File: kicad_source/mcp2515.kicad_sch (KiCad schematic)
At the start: 14 parts, among them CN4 GH_SM04B-GHS-TB, CN5 GH_SM04B-GHS-TB, U8 MCP2515, U9 SN65HVD232, Y1 16MHz

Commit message: started first placement
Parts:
- renumbered C3 to C5, C7 to C6, C8 to C7, C4 to C8, CN4 to CN10, CN5 to CN11, D2 to D3, R1 to R23, R2 to R24, R3 to R25, U8 to U2, U9 to U3
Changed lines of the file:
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@@
   (symbol (lib_id "OpenCyphalPicoBase-rescue:MCP2515-IC_transceiver_can") (at 127 55.88 0) (unit 1)
     (in_bom yes) (on_board yes)
-    (property "Reference" "U8" (id 0) (at 127 37.465 0))
+    (property "Reference" "U2" (id 0) (at 127 37.465 0))
     (property "Value" "MCP2515" (id 1) (at 127 39.7764 0))
     (property "Footprint" "Package_SO:SOIC-18W_7.5x11.6mm_P1.27mm" (id 2) (at 127 55.88 0)
@@
   (symbol (lib_id "Device:C_Small") (at 162.56 46.99 0) (unit 1)
     (in_bom yes) (on_board yes)
-    (property "Reference" "C3" (id 0) (at 164.8968 45.8216 0)
+    (property "Reference" "C5" (id 0) (at 164.8968 45.8216 0)
       (effects (font (size 1.27 1.27)) (justify left))
     )
@@
   (symbol (lib_id "OpenCyphalPicoBase-rescue:+3.3V-power-supply") (at 162.56 41.91 0) (unit 1)
     (in_bom yes) (on_board yes)
-    (property "Reference" "#PWR025" (id 0) (at 162.56 45.72 0)
+    (property "Reference" "#PWR052" (id 0) (at 162.56 45.72 0)
       (effects (font (size 1.27 1.27)) hide)
     )
@@
   (symbol (lib_id "OpenCyphalPicoBase-rescue:GND-power-supply") (at 162.56 50.8 0) (unit 1)
     (in_bom yes) (on_board yes)
-    (property "Reference" "#PWR026" (id 0) (at 162.56 57.15 0)
+    (property "Reference" "#PWR053" (id 0) (at 162.56 57.15 0)
       (effects (font (size 1.27 1.27)) hide)
     )
@@
   (symbol (lib_id "OpenCyphalPicoBase-rescue:GND-power-supply") (at 170.18 86.36 0) (unit 1)
     (in_bom yes) (on_board yes)
-    (property "Reference" "#PWR027" (id 0) (at 170.18 92.71 0)
+    (property "Reference" "#PWR055" (id 0) (at 170.18 92.71 0)
       (effects (font (size 1.27 1.27)) hide)
     )
@@
   (symbol (lib_id "Device:R_Small") (at 87.63 38.1 0) (unit 1)
     (in_bom yes) (on_board yes)
-    (property "Reference" "R3" (id 0) (at 89.1286 36.9316 0)
+    (property "Reference" "R25" (id 0) (at 89.1286 36.9316 0)
       (effects (font (size 1.27 1.27)) (justify left))
     )
@@
   (symbol (lib_id "OpenCyphalPicoBase-rescue:+3.3V-power-supply") (at 87.63 34.29 0) (unit 1)
     (in_bom yes) (on_board yes)
-    (property "Reference" "#PWR024" (id 0) (at 87.63 38.1 0)
+    (property "Reference" "#PWR051" (id 0) (at 87.63 38.1 0)
       (effects (font (size 1.27 1.27)) hide)
     )
@@
   (symbol (lib_id "Device:R_Small") (at 80.01 38.1 0) (unit 1)
     (in_bom yes) (on_board yes)
-    (property "Reference" "R2" (id 0) (at 81.5086 36.9316 0)
+    (property "Reference" "R24" (id 0) (at 81.5086 36.9316 0)
       (effects (font (size 1.27 1.27)) (justify left))
     )
@@
   (symbol (lib_id "OpenCyphalPicoBase-rescue:+3.3V-power-supply") (at 80.01 34.29 0) (unit 1)
     (in_bom yes) (on_board yes)
-    (property "Reference" "#PWR023" (id 0) (at 80.01 38.1 0)
+    (property "Reference" "#PWR050" (id 0) (at 80.01 38.1 0)
       (effects (font (size 1.27 1.27)) hide)
     )
@@
   (symbol (lib_id "Device:R_Small") (at 72.39 38.1 0) (unit 1)
     (in_bom yes) (on_board yes)
-    (property "Reference" "R1" (id 0) (at 73.8886 36.9316 0)
+    (property "Reference" "R23" (id 0) (at 73.8886 36.9316 0)
       (effects (font (size 1.27 1.27)) (justify left))
     )
@@
   (symbol (lib_id "OpenCyphalPicoBase-rescue:+3.3V-power-supply") (at 72.39 34.29 0) (unit 1)
     (in_bom yes) (on_board yes)
-    (property "Reference" "#PWR022" (id 0) (at 72.39 38.1 0)
+    (property "Reference" "#PWR049" (id 0) (at 72.39 38.1 0)
       (effects (font (size 1.27 1.27)) hide)
     )
@@
   (symbol (lib_id "OpenCyphalPicoBase-rescue:SN65HVD232-CAN-transceiver") (at 210.82 66.04 0) (unit 1)
     (in_bom yes) (on_board yes)
-    (property "Reference" "U9" (id 0) (at 224.155 43.5102 0)
+    (property "Reference" "U3" (id 0) (at 224.155 43.5102 0)
       (effects (font (size 1.524 1.524)))
     )
@@
   (symbol (lib_id "Device:C_Small") (at 198.12 45.72 0) (unit 1)
     (in_bom yes) (on_board yes)
-    (property "Reference" "C4" (id 0) (at 200.4568 44.5516 0)
+    (property "Reference" "C8" (id 0) (at 200.4568 44.5516 0)
       (effects (font (size 1.27 1.27)) (justify left))
     )
@@
   (symbol (lib_id "OpenCyphalPicoBase-rescue:+3.3V-power-supply") (at 198.12 40.64 0) (unit 1)
     (in_bom yes) (on_board yes)
-    (property "Reference" "#PWR028" (id 0) (at 198.12 44.45 0)
+    (property "Reference" "#PWR058" (id 0) (at 198.12 44.45 0)
       (effects (font (size 1.27 1.27)) hide)
     )
@@
   (symbol (lib_id "OpenCyphalPicoBase-rescue:GND-power-supply") (at 198.12 49.53 0) (unit 1)
     (in_bom yes) (on_board yes)
-    (property "Reference" "#PWR029" (id 0) (at 198.12 55.88 0)
+    (property "Reference" "#PWR059" (id 0) (at 198.12 55.88 0)
       (effects (font (size 1.27 1.27)) hide)
     )
@@
   (symbol (lib_id "OpenCyphalPicoBase-rescue:GND-power-supply") (at 209.55 63.5 0) (unit 1)
     (in_bom yes) (on_board yes)
-    (property "Reference" "#PWR030" (id 0) (at 209.55 69.85 0)
+    (property "Reference" "#PWR060" (id 0) (at 209.55 69.85 0)
       (effects (font (size 1.27 1.27)) hide)
     )
@@
   (symbol (lib_id "OpenCyphalPicoBase-rescue:CONN_01X04-mechanical-connectors") (at 223.52 106.68 0) (unit 1)
     (in_bom yes) (on_board yes)
-    (property "Reference" "CN4" (id 0) (at 225.5012 105.6386 0)
+    (property "Reference" "CN10" (id 0) (at 225.5012 105.6386 0)
       (effects (font (size 1.27 1.27)) (justify left))
     )
@@
   (symbol (lib_id "OpenCyphalPicoBase-rescue:GND-power-supply") (at 215.9 113.03 0) (unit 1)
     (in_bom yes) (on_board yes)
-    (property "Reference" "#PWR036" (id 0) (at 215.9 119.38 0)
+    (property "Reference" "#PWR061" (id 0) (at 215.9 119.38 0)
       (effects (font (size 1.27 1.27)) hide)
     )
@@
   (symbol (lib_id "OpenCyphalPicoBase-rescue:CONN_01X04-mechanical-connectors") (at 223.52 130.81 0) (unit 1)
     (in_bom yes) (on_board yes)
-    (property "Reference" "CN5" (id 0) (at 225.5012 129.7686 0)
+    (property "Reference" "CN11" (id 0) (at 225.5012 129.7686 0)
       (effects (font (size 1.27 1.27)) (justify left))
     )
@@
   (symbol (lib_id "OpenCyphalPicoBase-rescue:GND-power-supply") (at 215.9 137.16 0) (unit 1)
     (in_bom yes) (on_board yes)
-    (property "Reference" "#PWR037" (id 0) (at 215.9 143.51 0)
+    (property "Reference" "#PWR062" (id 0) (at 215.9 143.51 0)
       (effects (font (size 1.27 1.27)) hide)
     )
@@
   (symbol (lib_id "Device:D_Schottky_Small") (at 220.98 156.21 0) (unit 1)
     (in_bom yes) (on_board yes)
-    (property "Reference" "D2" (id 0) (at 220.98 151.003 0))
+    (property "Reference" "D3" (id 0) (at 220.98 151.003 0))
     (property "Value" "MBR0530T1G" (id 1) (at 220.98 153.3144 0))
     (property "Footprint" "Diode_SMD:D_SOD-123" (id 2) (at 220.98 156.21 90)
@@
   (symbol (lib_id "Device:C_Small") (at 176.53 85.09 0) (unit 1)
     (in_bom yes) (on_board yes)
-    (property "Reference" "C8" (id 0) (at 178.8668 83.9216 0)
+    (property "Reference" "C7" (id 0) (at 178.8668 83.9216 0)
       (effects (font (size 1.27 1.27)) (justify left))
     )
@@
   (symbol (lib_id "Device:C_Small") (at 163.83 85.09 0) (mirror y) (unit 1)
     (in_bom yes) (on_board yes)
-    (property "Reference" "C7" (id 0) (at 161.4932 83.9216 0)
+    (property "Reference" "C6" (id 0) (at 161.4932 83.9216 0)
       (effects (font (size 1.27 1.27)) (justify left))
     )
@@
   (symbol (lib_id "OpenCyphalPicoBase-rescue:GND-power-supply") (at 163.83 88.9 0) (unit 1)
     (in_bom yes) (on_board yes)
-    (property "Reference" "#PWR034" (id 0) (at 163.83 95.25 0)
+    (property "Reference" "#PWR054" (id 0) (at 163.83 95.25 0)
       (effects (font (size 1.27 1.27)) hide)
     )
@@
   (symbol (lib_id "OpenCyphalPicoBase-rescue:GND-power-supply") (at 176.53 88.9 0) (unit 1)
     (in_bom yes) (on_board yes)
-    (property "Reference" "#PWR035" (id 0) (at 176.53 95.25 0)
+    (property "Reference" "#PWR056" (id 0) (at 176.53 95.25 0)
       (effects (font (size 1.27 1.27)) hide)
     )
@@
   (symbol (lib_id "OpenCyphalPicoBase-rescue:GND-power-supply") (at 243.84 45.72 0) (unit 1)
     (in_bom yes) (on_board yes)
-    (property "Reference" "#PWR0102" (id 0) (at 243.84 52.07 0)
+    (property "Reference" "#PWR063" (id 0) (at 243.84 52.07 0)
       (effects (font (size 1.27 1.27)) hide)
     )
@@
   (symbol (lib_id "power:+5V") (at 195.58 154.94 0) (unit 1)
     (in_bom yes) (on_board yes) (fields_autoplaced)
-    (property "Reference" "#PWR?" (id 0) (at 195.58 158.75 0)
-      (effects (font (size 1.27 1.27)) hide)
-    )
+    (property "Reference" "#PWR057" (id 0) (at 195.58 158.75 0)
+      (effects (font (size 1.27 1.27)) hide)
+    )

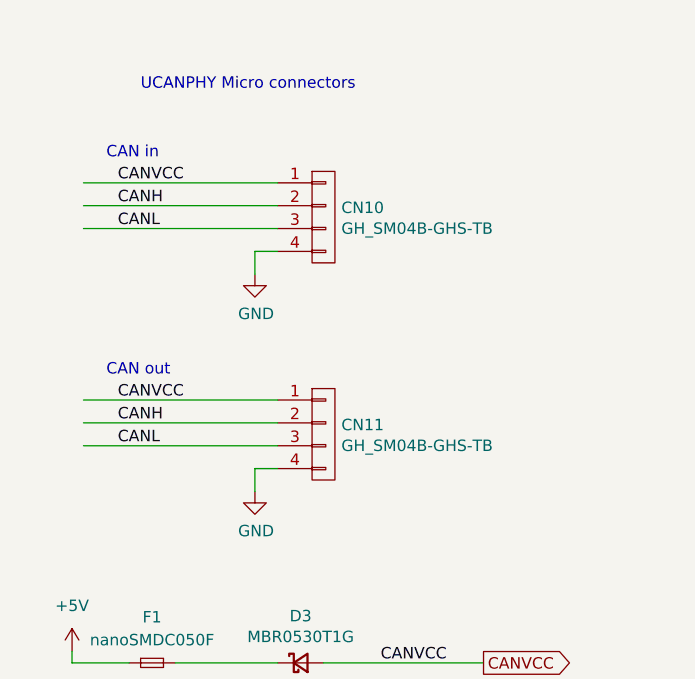
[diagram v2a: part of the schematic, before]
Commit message: added mounting pads, beautified layout, run DRC
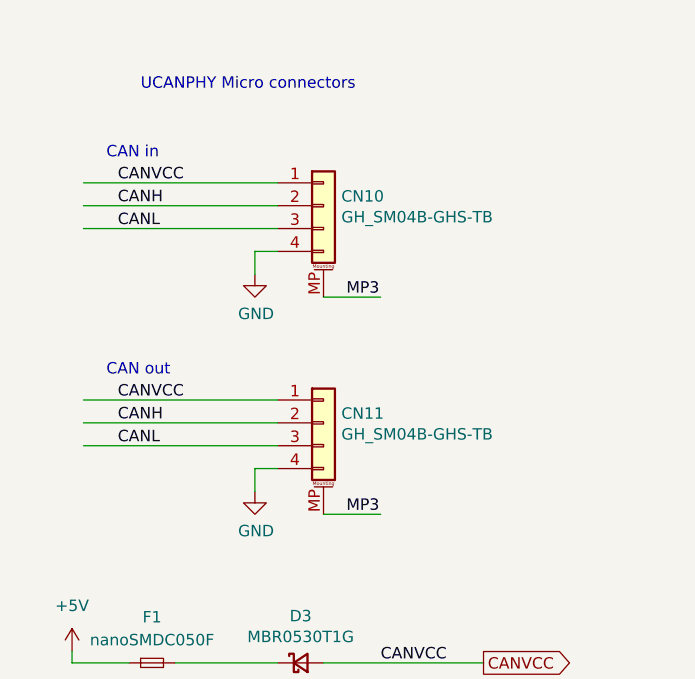
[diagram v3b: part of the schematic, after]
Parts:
- CN10, CN11: symbol OpenCyphalPicoBase-rescue:CONN_01X04-mechanical-connectors -> Connector_Generic_MountingPin:Conn_01x04_MountingPin
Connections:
- new net MP3: CN10.MP (MountPin), CN11.MP (MountPin)
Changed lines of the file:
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@@
   (title_block
     (title "OpenCyphalServoController12")
-    (date "2023-02-03")
+    (date "2023-02-04")
     (rev "0.1")
     (company "generationmake")
@@
     (stroke (width 0) (type default) (color 0 0 0 0))
   )
+  (wire (pts (xy 223.52 115.57) (xy 229.87 115.57))
+    (stroke (width 0) (type default) (color 0 0 0 0))
+  )
   (wire (pts (xy 162.56 50.8) (xy 162.56 49.53))
     (stroke (width 0) (type default) (color 0 0 0 0))
@@
     (stroke (width 0) (type default) (color 0 0 0 0))
   )
+  (wire (pts (xy 223.52 139.7) (xy 229.87 139.7))
+    (stroke (width 0) (type default) (color 0 0 0 0))
+  )
   (wire (pts (xy 91.44 58.42) (xy 113.03 58.42))
     (stroke (width 0) (type default) (color 0 0 0 0))
@@
     (effects (font (size 1.27 1.27)) (justify left bottom))
   )
+  (label "MP3" (at 226.06 115.57 0)
+    (effects (font (size 1.27 1.27)) (justify left bottom))
+  )
   (label "MCP2515_TX2RTS" (at 92.71 68.58 0)
     (effects (font (size 1.27 1.27)) (justify left bottom))
@@
   )
   (label "MOSI" (at 92.71 50.8 0)
+    (effects (font (size 1.27 1.27)) (justify left bottom))
+  )
+  (label "MP3" (at 226.06 139.7 0)
     (effects (font (size 1.27 1.27)) (justify left bottom))
   )
@@
     (pin "1")
   )
-  (symbol (lib_id "OpenCyphalPicoBase-rescue:CONN_01X04-mechanical-connectors") (at 223.52 106.68 0) (unit 1)
-    (in_bom yes) (on_board yes)
-    (property "Reference" "CN10" (id 0) (at 225.5012 105.6386 0)
-      (effects (font (size 1.27 1.27)) (justify left))
-    )
-    (property "Value" "GH_SM04B-GHS-TB" (id 1) (at 225.5012 107.95 0)
-      (effects (font (size 1.27 1.27)) (justify left))
-    )
-    (property "Footprint" "Connector_JST:JST_GH_SM04B-GHS-TB_1x04-1MP_P1.25mm_Horizontal" (id 2) (at 223.52 106.68 0)
-      (effects (font (size 1.27 1.27)) hide)
-    )
-    (property "Datasheet" "" (id 3) (at 223.52 106.68 0))
+  (symbol (lib_id "Connector_Generic_MountingPin:Conn_01x04_MountingPin") (at 223.52 105.41 0) (unit 1)
+    (in_bom yes) (on_board yes)
+    (property "Reference" "CN10" (id 0) (at 225.5012 104.3686 0)
+      (effects (font (size 1.27 1.27)) (justify left))
+    )
+    (property "Value" "GH_SM04B-GHS-TB" (id 1) (at 225.5012 106.68 0)
+      (effects (font (size 1.27 1.27)) (justify left))
+    )
+    (property "Footprint" "Connector_JST:JST_GH_SM04B-GHS-TB_1x04-1MP_P1.25mm_Horizontal" (id 2) (at 223.52 105.41 0)
+      (effects (font (size 1.27 1.27)) hide)
+    )
+    (property "Datasheet" "~" (id 3) (at 223.52 105.41 0)
+      (effects (font (size 1.27 1.27)) hide)
+    )
     (pin "1")
     (pin "2")
     (pin "3")
     (pin "4")
+    (pin "MP")
   )
   (symbol (lib_id "OpenCyphalPicoBase-rescue:GND-power-supply") (at 215.9 113.03 0) (unit 1)
@@
     (pin "1")
   )
-  (symbol (lib_id "OpenCyphalPicoBase-rescue:CONN_01X04-mechanical-connectors") (at 223.52 130.81 0) (unit 1)
-    (in_bom yes) (on_board yes)
-    (property "Reference" "CN11" (id 0) (at 225.5012 129.7686 0)
-      (effects (font (size 1.27 1.27)) (justify left))
-    )
-    (property "Value" "GH_SM04B-GHS-TB" (id 1) (at 225.5012 132.08 0)
-      (effects (font (size 1.27 1.27)) (justify left))
-    )
-    (property "Footprint" "Connector_JST:JST_GH_SM04B-GHS-TB_1x04-1MP_P1.25mm_Horizontal" (id 2) (at 223.52 130.81 0)
-      (effects (font (size 1.27 1.27)) hide)
-    )
-    (property "Datasheet" "" (id 3) (at 223.52 130.81 0))
+  (symbol (lib_id "Connector_Generic_MountingPin:Conn_01x04_MountingPin") (at 223.52 129.54 0) (unit 1)
+    (in_bom yes) (on_board yes)
+    (property "Reference" "CN11" (id 0) (at 225.5012 128.4986 0)
+      (effects (font (size 1.27 1.27)) (justify left))
+    )
+    (property "Value" "GH_SM04B-GHS-TB" (id 1) (at 225.5012 130.81 0)
+      (effects (font (size 1.27 1.27)) (justify left))
+    )
+    (property "Footprint" "Connector_JST:JST_GH_SM04B-GHS-TB_1x04-1MP_P1.25mm_Horizontal" (id 2) (at 223.52 129.54 0)
+      (effects (font (size 1.27 1.27)) hide)
+    )
+    (property "Datasheet" "~" (id 3) (at 223.52 129.54 0)
+      (effects (font (size 1.27 1.27)) hide)
+    )
     (pin "1")
     (pin "2")
     (pin "3")
     (pin "4")
+    (pin "MP")
   )
   (symbol (lib_id "OpenCyphalPicoBase-rescue:GND-power-supply") (at 215.9 137.16 0) (unit 1)
